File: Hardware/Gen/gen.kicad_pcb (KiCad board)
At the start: 2 copper layers, 4 parts, among them J1 Screw_Terminal_01x03

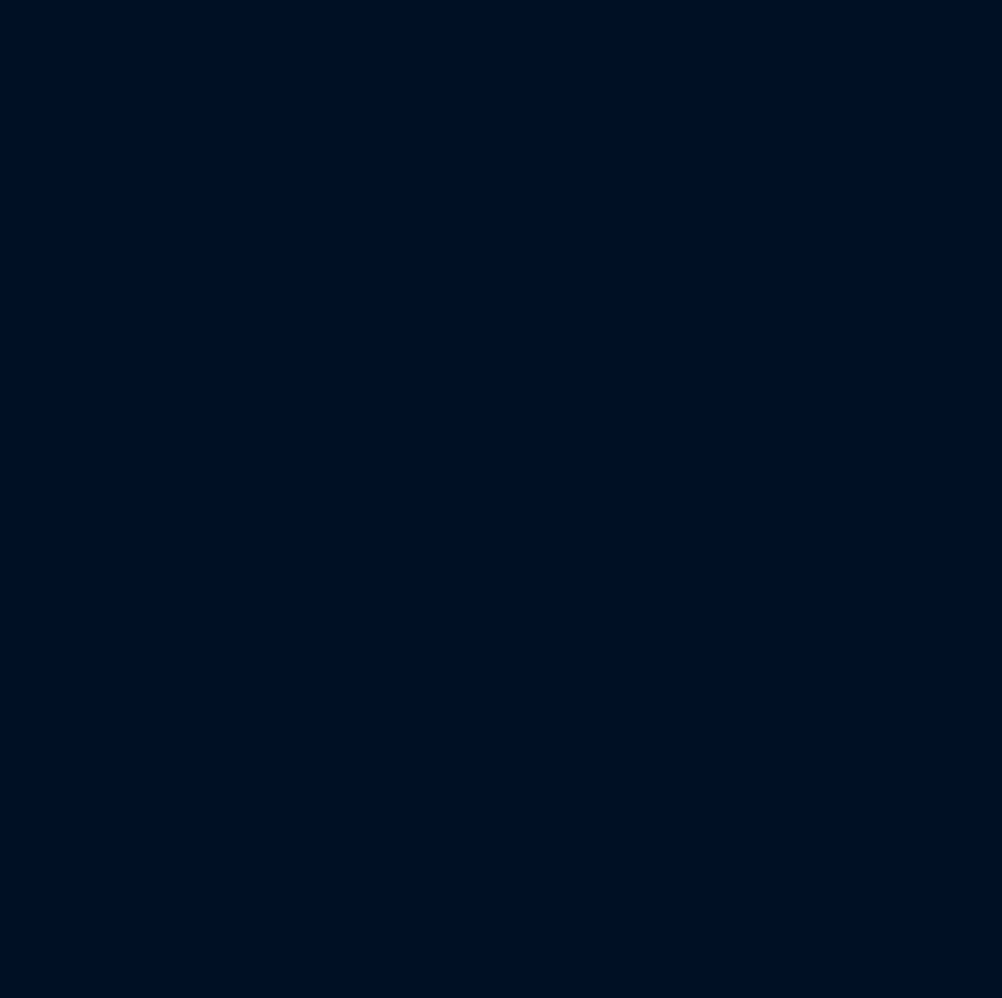
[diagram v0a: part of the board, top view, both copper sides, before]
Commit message: Gen: Rev 1 schem done, footprints assignment underway
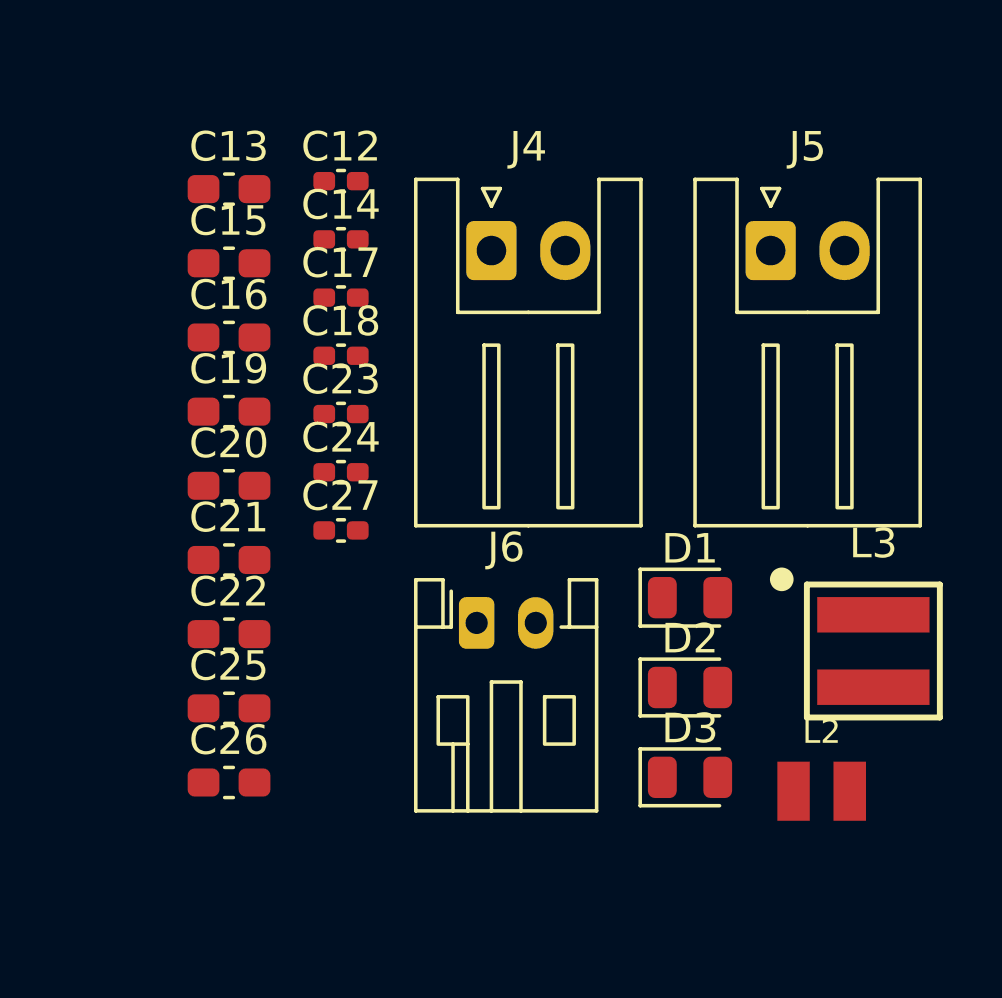
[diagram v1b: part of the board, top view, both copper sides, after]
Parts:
- added C12: 100nF, Capacitor_SMD:C_0402_1005Metric_Pad0.74x0.62mm_HandSolder, F.Cu at (205.0, 73.5)
- added C13: 15uF, Capacitor_SMD:C_0603_1608Metric_Pad1.08x0.95mm_HandSolder, F.Cu at (201.2, 73.8)
- added C14: 100nF, Capacitor_SMD:C_0402_1005Metric_Pad0.74x0.62mm_HandSolder, F.Cu at (205.0, 75.5)
- added C15: 4.7uF, Capacitor_SMD:C_0603_1608Metric_Pad1.08x0.95mm_HandSolder, F.Cu at (201.2, 76.3)
- added C16: 10uF, Capacitor_SMD:C_0603_1608Metric_Pad1.08x0.95mm_HandSolder, F.Cu at (201.2, 78.8)
- added C17: 100nF, Capacitor_SMD:C_0402_1005Metric_Pad0.74x0.62mm_HandSolder, F.Cu at (205.0, 77.4)
- added C18: 100nF, Capacitor_SMD:C_0402_1005Metric_Pad0.74x0.62mm_HandSolder, F.Cu at (205.0, 79.4)
- added C19: 22uF, Capacitor_SMD:C_0603_1608Metric_Pad1.08x0.95mm_HandSolder, F.Cu at (201.2, 81.3)
- added C20: 22uF, Capacitor_SMD:C_0603_1608Metric_Pad1.08x0.95mm_HandSolder, F.Cu at (201.2, 83.8)
- added C21: 10uF, Capacitor_SMD:C_0603_1608Metric_Pad1.08x0.95mm_HandSolder, F.Cu at (201.2, 86.3)
- added C22: 10uF, Capacitor_SMD:C_0603_1608Metric_Pad1.08x0.95mm_HandSolder, F.Cu at (201.2, 88.8)
- added C23: 100nF, Capacitor_SMD:C_0402_1005Metric_Pad0.74x0.62mm_HandSolder, F.Cu at (205.0, 81.4)
- added C24: 100nF, Capacitor_SMD:C_0402_1005Metric_Pad0.74x0.62mm_HandSolder, F.Cu at (205.0, 83.3)
- added C25: 10uF, Capacitor_SMD:C_0603_1608Metric_Pad1.08x0.95mm_HandSolder, F.Cu at (201.2, 91.3)
- added C26: 10uF, Capacitor_SMD:C_0603_1608Metric_Pad1.08x0.95mm_HandSolder, F.Cu at (201.2, 93.8)
- added C27: 100nF, Capacitor_SMD:C_0402_1005Metric_Pad0.74x0.62mm_HandSolder, F.Cu at (205.0, 85.3)
- added D1: LED, LED_SMD:LED_0805_2012Metric, F.Cu at (216.8, 87.6)
- added D2: LED, LED_SMD:LED_0805_2012Metric, F.Cu at (216.8, 90.6)
- added D3: LED, LED_SMD:LED_0805_2012Metric, F.Cu at (216.8, 93.7)
- added J4: GAMEN, Connector_JST:JST_XH_S2B-XH-A_1x02_P2.50mm_Horizontal, F.Cu at (210.1, 75.8)
- added J5: SHORI, Connector_JST:JST_XH_S2B-XH-A_1x02_P2.50mm_Horizontal, F.Cu at (219.5, 75.8)
- added J6: MAE, Connector_JST:JST_PH_S2B-PH-K_1x02_P2.00mm_Horizontal, F.Cu at (209.6, 88.4)
- added L2: 68uH, My footprints:WE-LQS_2512, F.Cu at (221.2, 94.1)
- added L3: 5.6uH, My footprints:WE-XHMI_4040, F.Cu at (223.0, 89.4)

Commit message: Gen: Layout rev 1 done and routing started
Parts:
- added H1: MountingHole, MountingHole:MountingHole_4mm, F.Cu at (74.9, 85.6)
- added H2: MountingHole, MountingHole:MountingHole_4mm, F.Cu at (78.0, 138.1)
- added H3: MountingHole, MountingHole:MountingHole_4mm, F.Cu at (219.4, 85.7)
- added J2: XLR4, TerminalBlock_CUI:TerminalBlock_CUI_TB007-508-04_1x04_P5.08mm_Horizontal, F.Cu at (208.8, 117.9)
- added J3: XLR3, TerminalBlock_CUI:TerminalBlock_CUI_TB007-508-03_1x03_P5.08mm_Horizontal, F.Cu at (208.8, 135.3)
- added R10: 30, Resistor_SMD:R_0402_1005Metric_Pad0.72x0.64mm_HandSolder, F.Cu at (193.0, 112.0)
- added R11: 52.3K, Resistor_SMD:R_0603_1608Metric_Pad0.98x0.95mm_HandSolder, F.Cu at (195.0, 112.4)
- added R12: 10K, Resistor_SMD:R_0402_1005Metric_Pad0.72x0.64mm_HandSolder, F.Cu at (195.0, 115.4)
- added R13: 300, Resistor_SMD:R_0402_1005Metric_Pad0.72x0.64mm_HandSolder, F.Cu at (196.8, 97.5)
- added R14: 680, Resistor_SMD:R_0402_1005Metric_Pad0.72x0.64mm_HandSolder, F.Cu at (212.0, 94.8)
- added R15: 2.2K, Resistor_SMD:R_0805_2012Metric_Pad1.20x1.40mm_HandSolder, F.Cu at (178.1, 134.5)
- added R5: 178K, Resistor_SMD:R_0603_1608Metric_Pad0.98x0.95mm_HandSolder, F.Cu at (195.0, 127.2)
- added R6: 22.1K, Resistor_SMD:R_0603_1608Metric_Pad0.98x0.95mm_HandSolder, F.Cu at (195.0, 130.5)
- added R7: 1.37M, Resistor_SMD:R_0603_1608Metric_Pad0.98x0.95mm_HandSolder, F.Cu at (191.7, 124.7)
- added R8: 255K, Resistor_SMD:R_0603_1608Metric_Pad0.98x0.95mm_HandSolder, F.Cu at (193.1, 124.6)
- added R9: 100K, Resistor_SMD:R_0603_1608Metric_Pad0.98x0.95mm_HandSolder, F.Cu at (189.6, 117.9)
- added TP1: TestPoint, TestPoint:TestPoint_Pad_D2.5mm, F.Cu at (181.1, 91.0)
- added TP2: TestPoint, TestPoint:TestPoint_Pad_D2.5mm, F.Cu at (218.8, 94.3)
- added TP3: TestPoint, TestPoint:TestPoint_Pad_D2.5mm, F.Cu at (195.3, 136.4)
- added TP4: TestPoint, TestPoint:TestPoint_Pad_D2.5mm, F.Cu at (181.1, 84.3)
- added U1: TPS56339DDCT, Package_TO_SOT_SMD:SOT-23-6_Handsoldering, F.Cu at (190.6, 114.5)
- added U3: TPS560430YDBVR, Package_TO_SOT_SMD:SOT-23-6_Handsoldering, F.Cu at (191.6, 128.8)
- C23: footprint Capacitor_SMD:C_0402_1005Metric_Pad0.74x0.62mm_HandSolder -> Capacitor_SMD:C_0603_1608Metric_Pad1.08x0.95mm_HandSolder
- moved C12 60.3 mm to (189.9, 131.8)
- moved D3 57.9 mm to (179.1, 137.6), turned to 180 degrees
- moved C14 57.7 mm to (187.8, 130.5), turned to 90 degrees
- moved C15 56.4 mm to (186.4, 130.7), turned to 90 degrees
- moved C23 56.0 mm to (201.9, 137.3), turned to 90 degrees
- moved C13 49.5 mm to (195.9, 122.9), turned to 180 degrees
- moved C22 48.5 mm to (200.4, 137.3), turned to 90 degrees
- moved L2 44.4 mm to (188.5, 124.2), turned to -90 degrees
- moved C17 38.9 mm to (188.0, 112.4), turned to -90 degrees
- moved C16 38.7 mm to (184.9, 113.8), turned to 90 degrees
- moved C2 37.3 mm to (171.3, 129.9)
- moved L3 35.5 mm to (192.1, 106.8), turned to -90 degrees
- moved C18 34.9 mm to (191.2, 111.5)
- moved C27 33.6 mm to (202.6, 118.8), turned to 90 degrees
- moved J5 32.7 mm to (190.5, 91.0), turned to 180 degrees
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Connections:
- C16 pad 1: Net-(U1-GND) -> GND
- C17 pad 1: Net-(U1-GND) -> GND
- C19 pad 1: Net-(U1-GND) -> GND
- C20 pad 1: Net-(U1-GND) -> GND
- C21 pad 1: Net-(U1-GND) -> GND
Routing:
- net /DC_OUT: track 0.00 -> 95.4 mm
- net +9V: track 0.00 -> 27.3 mm
- net Net-(U3-SW): track 0.00 -> 8.65 mm, vias 0 -> 2
- net Net-(U3-EN): track 0.00 -> 4.48 mm
- net Net-(U3-FB): track 0.00 -> 4.15 mm
- net GND: track 0.00 -> 2.99 mm, vias 0 -> 2
- net Net-(D3-A): track 0.00 -> 2.14 mm
- net Net-(U1-EN): track 0.00 -> 2.09 mm
- net Net-(U3-CB): track 0.00 -> 1.73 mm
- added copper zone on B.Cu, net GND
- added copper zone on F.Cu, net GND
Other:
- board outline added: 153.9 x 62.1 mm

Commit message: Gen: Layout and routing complete rev 1
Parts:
- moved H3 4.43 mm to (214.9, 85.7)
- moved PS1 3.91 mm to (126.0, 113.5)
- moved TP3 3.09 mm to (195.2, 139.5)
- moved C25 3.01 mm to (199.7, 108.0), turned to 90 degrees
- moved TP2 2.38 mm to (216.4, 94.9)
- moved TP1 1.90 mm to (183.0, 91.0)
- moved TP4 1.71 mm to (182.8, 84.4)
- moved C13 1.50 mm to (195.9, 124.4)
- moved C20 1.18 mm to (197.8, 108.0)
- moved C19 1.18 mm to (196.0, 108.0)
- moved C24 1.04 mm to (201.2, 108.0), turned to 90 degrees
- moved R15 0.93 mm to (178.2, 135.4)
- moved D3 0.79 mm to (179.2, 138.4)
- moved C18 0.76 mm to (191.2, 110.7)
- moved R12 0.49 mm to (194.5, 115.5)
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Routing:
- net +5V: track 0.00 -> 57.0 mm
- net +9V: track 27.3 -> 65.0 mm
- net GND: track 2.99 -> 18.0 mm, vias 2 -> 9
- net /ACL: track 0.00 -> 13.6 mm
- net /ACN: track 0.00 -> 12.2 mm
- net Net-(U1-FB): track 0.00 -> 7.69 mm, vias 0 -> 2
- net Net-(U1-SW): track 0.00 -> 6.34 mm
- net /DC_OUT: track 95.4 -> 101.0 mm
- net Net-(U1-BOOT): track 0.00 -> 3.78 mm
- net Net-(D1-A): track 0.00 -> 1.98 mm
- net Net-(D2-A): track 0.00 -> 1.92 mm
- net Net-(C18-Pad2): track 0.00 -> 1.59 mm
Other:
- board size 153.9 x 62.1 mm -> 149.6 x 62.2 mm

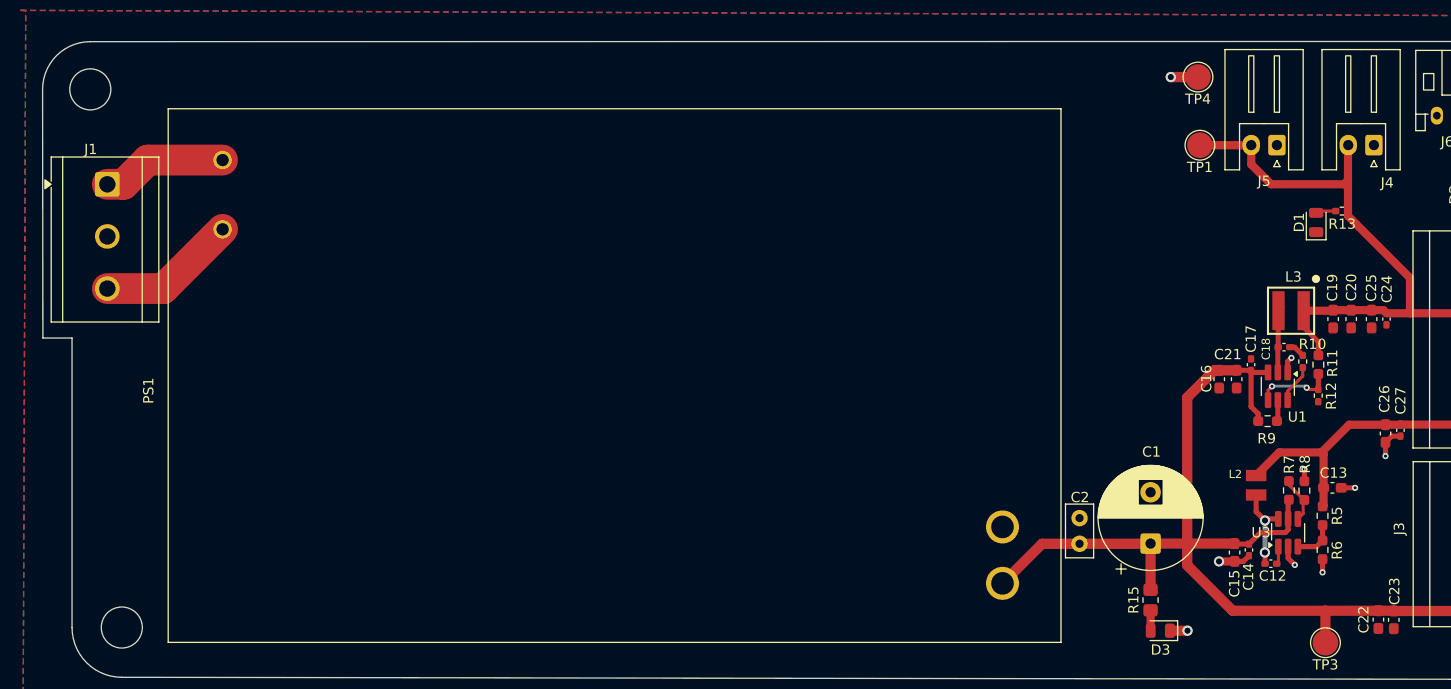
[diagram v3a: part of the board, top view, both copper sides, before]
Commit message: digikey order sheet wave forge 1 added
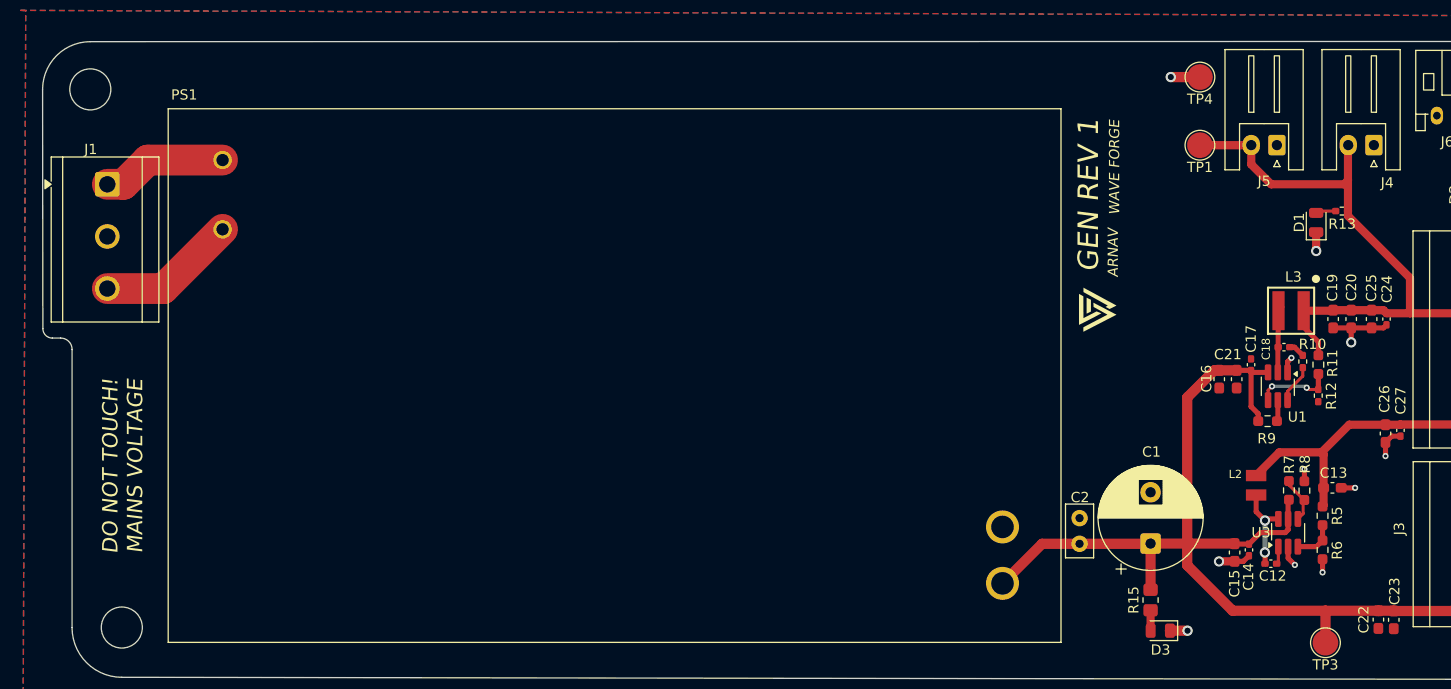
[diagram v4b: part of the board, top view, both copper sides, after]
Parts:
- added G***: LOGO, MyFootprints:logo, F.Cu at (172.0, 107.3)
- moved TP4 0.19 mm to (183.0, 84.4)
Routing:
- net GND: track 18.0 -> 26.6 mm, vias 9 -> 11
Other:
- outline, holes or cut-outs redrawn
- board text added: "ARNAV"
- board text added: "DO NOT TOUCH! MAINS VOLTAGE"
- board text added: "GEN REV 1"
- board text added: "WAVE FORGE"

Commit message: Gen: New Routing, More memes and better buck layouts (rev 2)
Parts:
- added G***: LOGO, My footprints:hands, F.Cu at (128.1, 114.7)
- added H3: MountingHole, MountingHole:MountingHole_4mm, F.Cu at (215.1, 141.9)
- added J7: Screw_Terminal_01x02, TerminalBlock_CUI:TerminalBlock_CUI_TB007-508-02_1x02_P5.08mm_Horizontal, F.Cu at (76.1, 125.8)
- moved R13 10.8 mm to (186.2, 95.6), turned to 90 degrees
- moved D1 9.88 mm to (184.5, 97.7)
- moved C24 8.32 mm to (195.8, 101.6), turned to -90 degrees
- moved C19 7.77 mm to (200.9, 102.0), turned to -90 degrees
- moved R6 7.08 mm to (197.3, 123.8)
- moved C14 6.92 mm to (190.8, 124.2)
- moved C15 6.92 mm to (189.4, 124.5)
- moved C12 6.59 mm to (193.2, 126.1)
- moved L2 6.47 mm to (193.6, 128.1), turned to 180 degrees
- moved C25 6.46 mm to (197.3, 102.0), turned to -90 degrees
- moved C20 6.17 mm to (199.2, 102.0), turned to -90 degrees
- moved R9 5.70 mm to (192.9, 113.3)
- moved U3 5.59 mm to (193.8, 123.7), turned to 180 degrees
- moved TP3 5.33 mm to (194.5, 134.2)
- moved R5 5.22 mm to (198.9, 123.8), turned to 90 degrees
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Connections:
- J1 pad 2: GND -> unconnected-(J1-Pin_2-Pad2)
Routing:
- net /DC_OUT: track 101.0 -> 10.9 mm
- net +9V: track 65.0 -> 0.00 mm
- net +5V: track 57.0 -> 0.00 mm
- net /ACL: track 13.6 -> 0.00 mm
- net /ACN: track 12.2 -> 0.00 mm
- net Net-(U3-SW): track 8.65 -> 3.32 mm, vias 2 -> 0
- net Net-(U1-FB): track 7.69 -> 3.44 mm, vias 2 -> 0
- net GND: track 26.6 -> 30.6 mm, vias 11 -> 113
- net Net-(U1-BOOT): track 3.78 -> 1.49 mm
- net Net-(U1-SW): track 6.34 -> 8.07 mm
- net Net-(U1-EN): track 2.09 -> 3.49 mm
- net Net-(U3-EN): track 4.48 -> 3.24 mm
- net Net-(U3-CB): track 1.73 -> 2.53 mm
- added copper zone on F.Cu, net +5V
- added copper zone on F.Cu, net +9V
- added copper zone on F.Cu, net /ACL
- added copper zone on F.Cu, net /ACN
- added copper zone on F.Cu, net /DC_OUT
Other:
- board size 149.6 x 62.2 mm -> 149.8 x 65.8 mm
- board text added: "GEN REV 2"
- board text removed: "DO NOT TOUCH! MAINS VOLTAGE"
- board text removed: "GEN REV 1"
